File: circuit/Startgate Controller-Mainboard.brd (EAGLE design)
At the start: 160 x 100 mm, 22 parts, among them IC1 MAX3490ESA, IC2 L293D, U2 HEF4066BT, U3 HEF4066BT, U4 HEF4066BT, U5 HEF4066BT, X1 RJ45-8L21-B

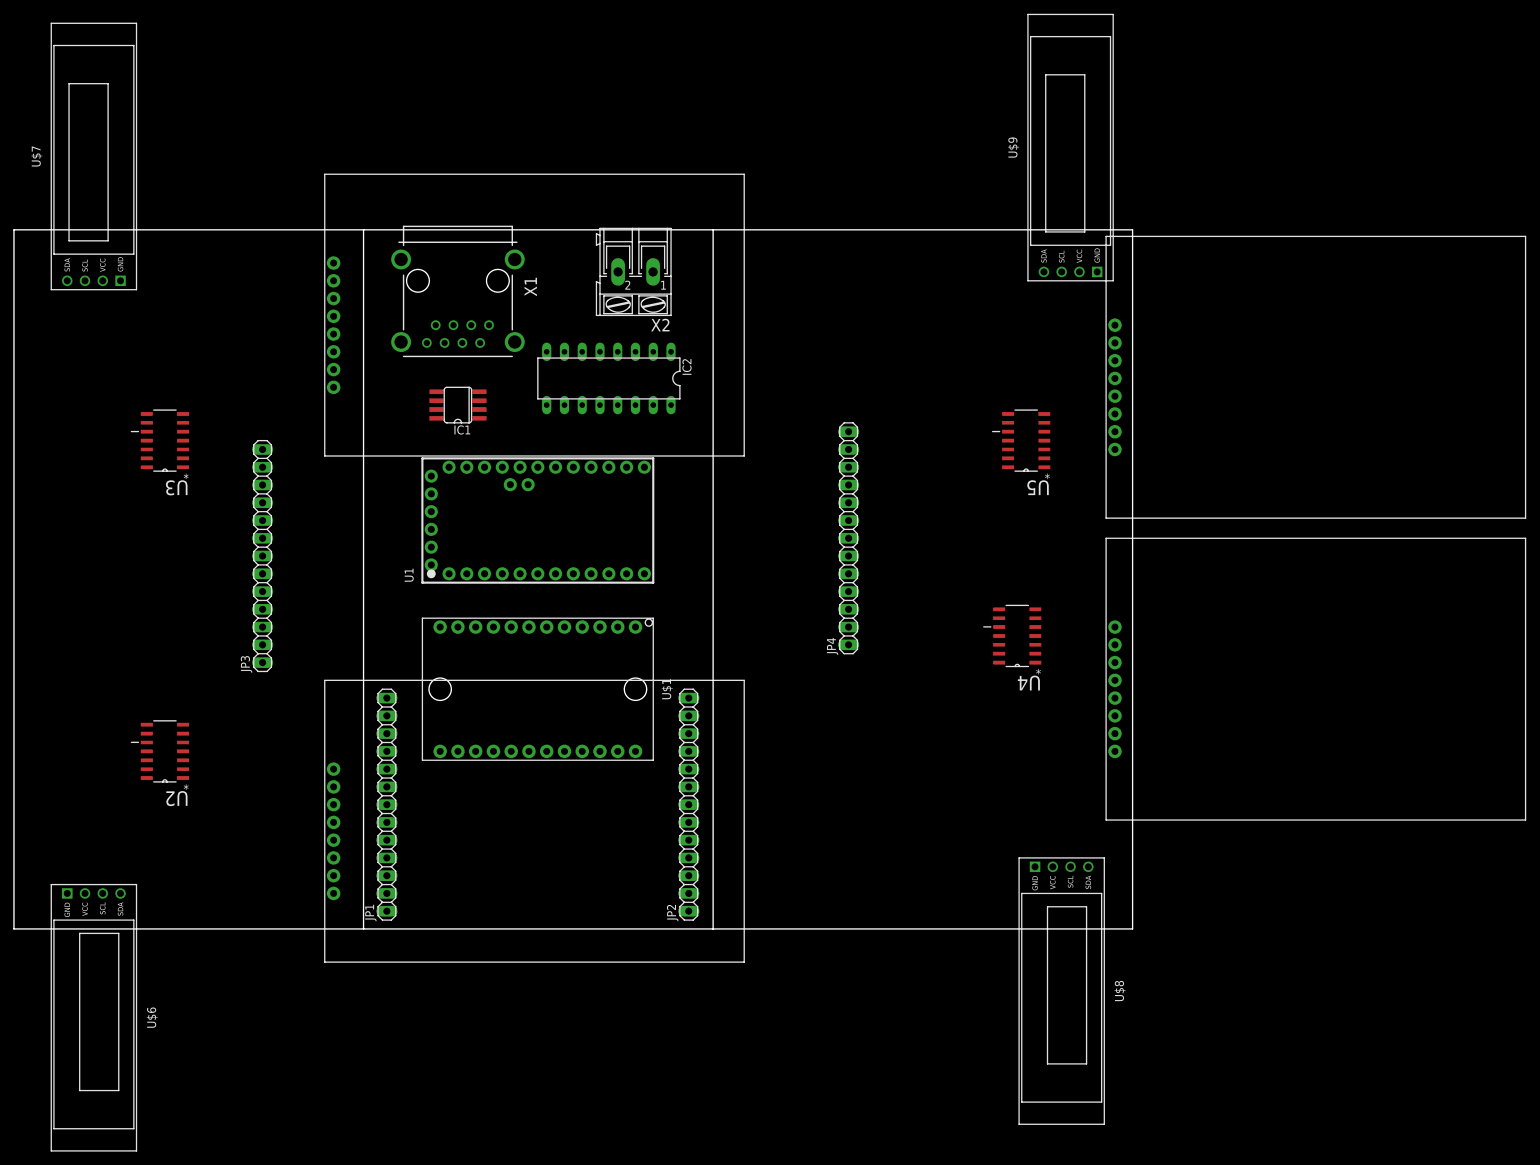
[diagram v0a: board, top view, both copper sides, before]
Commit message: add the circuitry for the startgate main- and daughterboards
The main startgate controller has been split up into main board
and daughterboards, to make it easier to send them to the board house.
The two daughterboards should be identical, so the next iteration will
skip one.
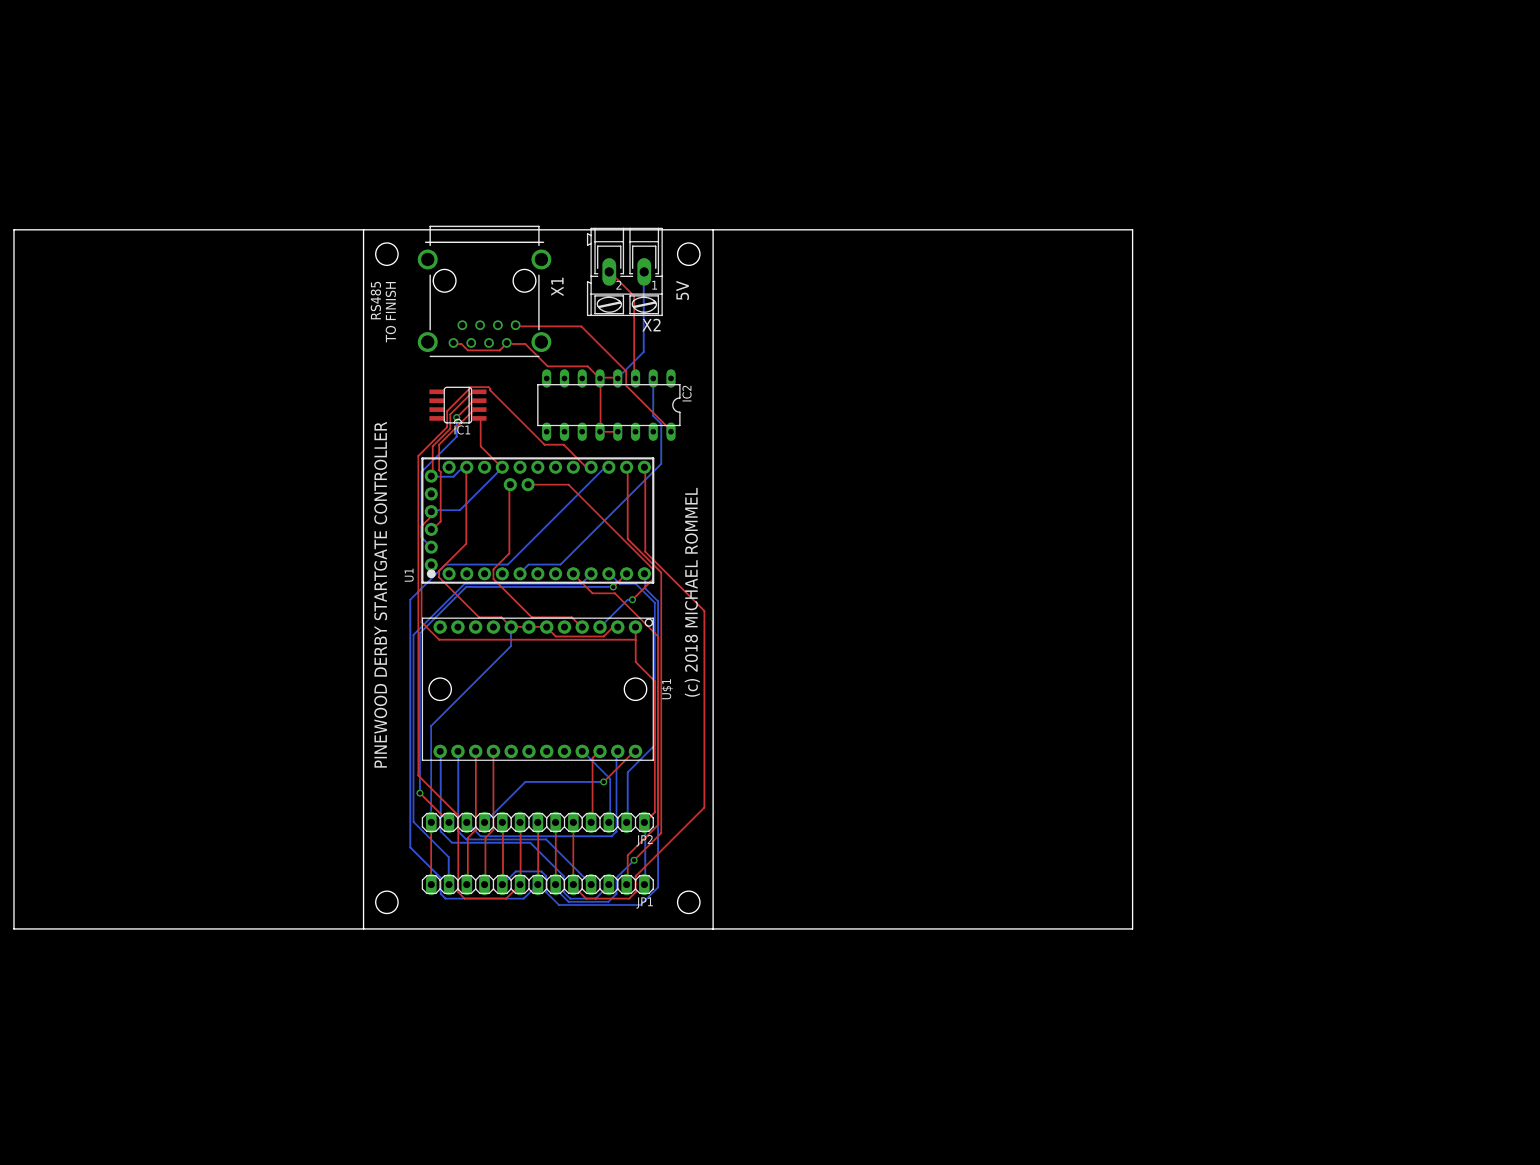
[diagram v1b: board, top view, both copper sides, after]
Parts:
- removed JP3, JP4: (no value), pinhead:1X13
- removed U$2, U$3, U$4, U$5: RFID-RC522, miro:RFID-RC522
- removed U$6, U$7, U$8, U$9: DISPLAY-OLED-128X32, diy-modules:DISPLAY-OLED-128X32
- removed U2, U3, U4, U5: HEF4066BT, NXP_By_element14_Batch_1:SOIC127P600X175-14N
- moved JP1 24.4 mm to (74.9, 6.35), turned to 180 degrees
- moved JP2 21.7 mm to (74.9, 15.2), turned to 180 degrees
- moved X1 3.81 mm to (67.3, 92.7)
- moved IC2 3.81 mm to (85.1, 74.9)
- moved X2 1.27 mm to (87.6, 94.0)
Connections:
- removed net MISO-OUT1: U$2.4, U2.10
- removed net MISO-OUT2: U$3.4, U3.10
- removed net MISO-OUT3: U$4.4, U4.10
- removed net MISO-OUT4: U$5.4, U5.10
- removed net MOSI-OUT1: U$2.3, U2.9
- removed net MOSI-OUT2: U$3.3, U3.9
- removed net MOSI-OUT3: U$4.3, U4.9
- removed net MOSI-OUT4: U$5.3, U5.9
- removed net SCK-OUT1: U$2.2, U2.3
- removed net SCK-OUT2: U$3.2, U3.3
- removed net SCK-OUT3: U$4.2, U4.3
- removed net SCK-OUT4: U$5.2, U5.3
- removed net SS-OUT1: U$2.1, U2.2
- removed net SS-OUT2: U$3.1, U3.2
- removed net SS-OUT3: U$4.1, U4.2
- removed net SS-OUT4: U$5.1, U5.2
- net +3V3: no longer JP3.1, JP4.1, U$2.8, U$3.8, U$4.8, U$5.8, U$6.2, U$7.2, U$8.2, U$9.2, U2.14, U3.14, U4.14, U5.14
- net ENA1: no longer JP3.2, U2.12, U2.13, U2.5, U2.6
- net ENA2: no longer JP3.12, U3.12, U3.13, U3.5, U3.6
- net ENA3: no longer JP4.2, U4.12, U4.13, U4.5, U4.6
- net ENA4: no longer JP4.12, U5.12, U5.13, U5.5, U5.6
- net GND: no longer JP3.13, JP4.13, U$2.6, U$3.6, U$4.6, U$5.6, U$6.1, U$7.1, U$8.1, U$9.1, U2.7, U3.7, U4.7, U5.7
- net MISO: no longer JP3.7, JP4.7, U2.11, U3.11, U4.11, U5.11
- net MOSI: no longer JP3.6, JP4.6, U2.8, U3.8, U4.8, U5.8
- net RST: no longer JP3.9, JP4.9, U$2.7, U$3.7, U$4.7, U$5.7
- net SCK: no longer JP3.8, JP4.8, U2.4, U3.4, U4.4, U5.4
- net SCL1: no longer JP3.4, U$6.3
- net SCL2: no longer JP3.10, U$7.3
- net SCL3: no longer JP4.4, U$8.3
- net SCL4: no longer JP4.10, U$9.3
- net SDA1: no longer JP3.3, U$6.4
- net SDA2: no longer JP3.11, U$7.4
- net SDA3: no longer JP4.3, U$8.4
- net SDA4: no longer JP4.11, U$9.4
- net SS: no longer JP3.5, JP4.5, U2.1, U3.1, U4.1, U5.1
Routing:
- net SCK: track 0.00 -> 118.8 mm
- net GND: track 0.00 -> 109.8 mm
- net +3V3: track 0.00 -> 108.0 mm
- net MISO: track 0.00 -> 104.1 mm
- net SS: track 0.00 -> 87.5 mm
- net MOSI: track 0.00 -> 85.2 mm, vias 0 -> 1
- net RST: track 0.00 -> 82.1 mm
- net ENA2: track 0.00 -> 66.8 mm
- net ENA4: track 0.00 -> 61.9 mm, vias 0 -> 2
- net N$13: track 0.00 -> 53.7 mm
- net ENA1: track 0.00 -> 53.3 mm
- net SDA1: track 0.00 -> 41.8 mm
- net ENA3: track 0.00 -> 41.4 mm
- net N$10: track 0.00 -> 39.4 mm
- net N$6: track 0.00 -> 34.8 mm, vias 0 -> 1
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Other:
- board text added: "(c) 2018 MICHAEL ROMMEL"
- board text added: "5V"
- board text added: "PINEWOOD DERBY STARTGATE CONTROLLER"
- board text added: "RS485 TO FINISH"
